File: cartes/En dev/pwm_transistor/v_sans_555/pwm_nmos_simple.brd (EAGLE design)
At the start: 27.6 x 43.2 mm, 16 parts, among them Q1 MOSFET-NCHANNELFQP30N06L, T1 2N2222

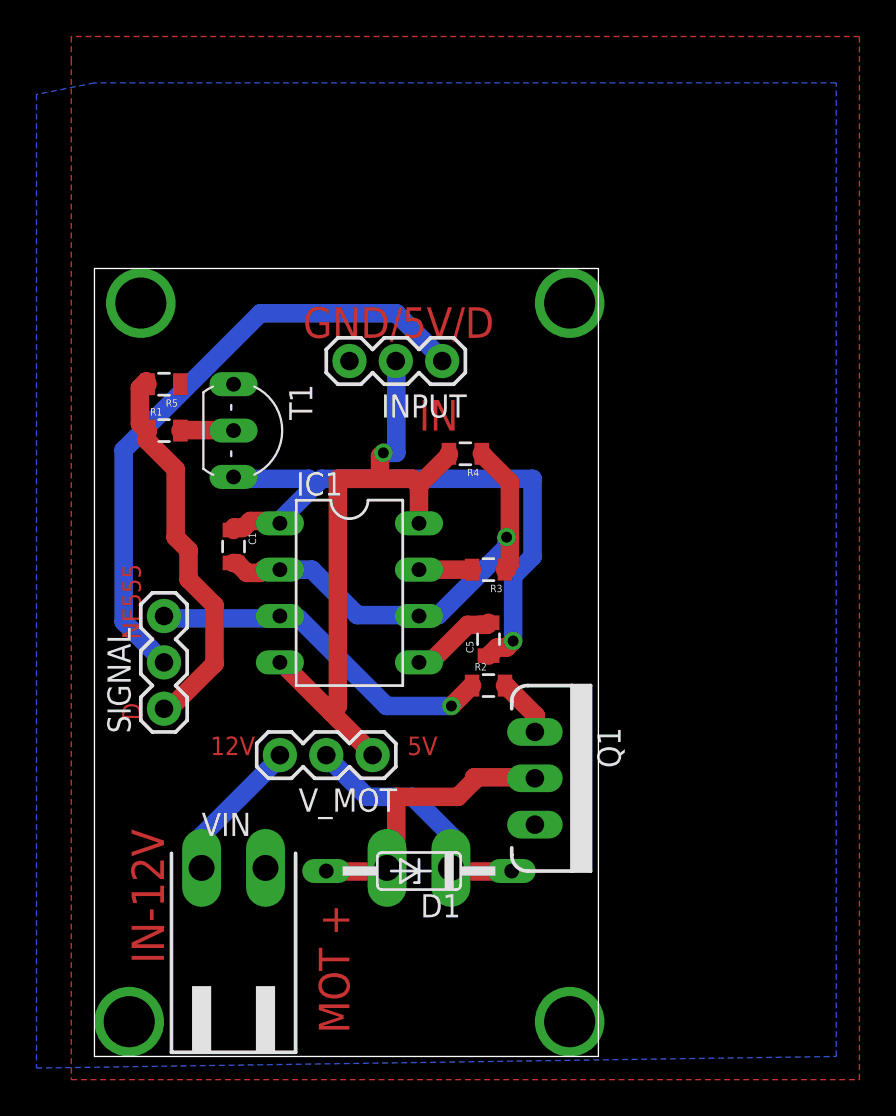
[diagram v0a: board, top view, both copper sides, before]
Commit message: carte mos pwm modifié
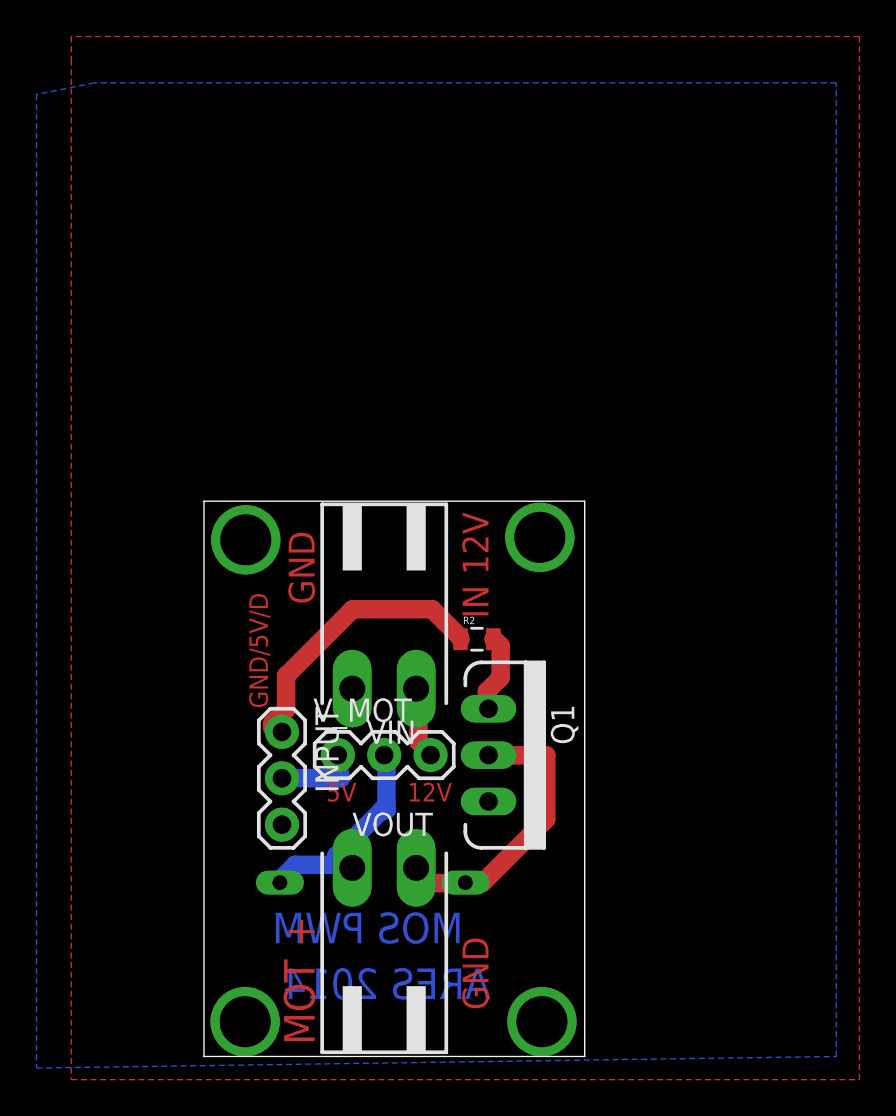
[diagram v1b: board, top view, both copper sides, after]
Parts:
- removed C1, C5: 22pF, SparkFun-Capacitors:0805
- removed IC1: (no value), SparkFun-AnalogIC:DIL-08
- removed R1: 1k, SparkFun-Resistors:0805
- removed R3, R4: (no value), SparkFun-Resistors:0805
- removed R5: 10k, SparkFun-Resistors:0805
- removed SIGNAL: (no value), SparkFun-Connectors:1X03
- removed T1: 2N2222, adafruit:TO92-EBC-OVAL
- moved INPUT 22.1 mm to (10.3, 17.8), turned to 270 degrees
- moved VIN 21.9 mm to (15.9, 25.4), turned to 180 degrees
- moved Q1 2.84 mm to (21.6, 16.5)
- moved D1 2.62 mm to (15.2, 9.53), flipped to the bottom
- moved R2 2.62 mm to (21.0, 22.9)
- moved VOUT 1.91 mm to (15.9, 5.08), flipped to the top
- moved V_MOT 1.90 mm to (13.3, 16.5), turned to 0 degrees
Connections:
- removed net ENABLE_555: C1.1, C5.1, IC1.1, T1.C
- removed net N$2: R1.2, T1.B
- removed net N$5: C1.2, IC1.2, IC1.6, R3.1, R4.1
- removed net N$6: IC1.7, R3.2
- removed net N$8: C5.2, IC1.5
- removed net SIG: INPUT.1, SIGNAL.2
- removed net SIG_555: R1.1, R5.2, SIGNAL.1
- net GND: no longer R5.1, T1.E
- net IN_MOS: now also INPUT.1; no longer IC1.3, SIGNAL.3
- net VCC: no longer IC1.4, IC1.8, R4.2
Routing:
- net SIG: track 34.2 -> 0.00 mm
- net ENABLE_555: track 33.6 -> 0.00 mm, vias 1 -> 0
- net VCC: track 36.5 -> 4.64 mm, vias 1 -> 0
- net N$5: track 25.8 -> 0.00 mm, vias 1 -> 0
- net SIG_555: track 21.3 -> 0.00 mm
- net N$8: track 4.78 -> 0.00 mm
- net 12V: track 7.95 -> 3.94 mm
- net IN_MOS: track 19.5 -> 15.5 mm, vias 1 -> 0
- net N$2: track 2.92 -> 0.00 mm
- net N$6: track 2.91 -> 0.00 mm
- net V+_MOT: track 14.0 -> 12.5 mm
- net N$3: track 3.31 -> 4.32 mm
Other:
- board size 27.6 x 43.2 mm -> 20.9 x 30.4 mm
- board text added: "ARES 2014"
- board text added: "GND"
- board text added: "IN 12V"
- board text added: "MOS PWM"
- board text removed: "D"
- board text removed: "IN"
- board text removed: "IN-12V"
- board text removed: "NE555"
